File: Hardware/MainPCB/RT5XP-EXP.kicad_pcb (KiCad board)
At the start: 4 copper layers, 153 x 78 mm, 145 parts, among them J1 Conn_Coaxial, J10 Conn_01x02_Male, J11 Conn_01x11_Male, J12 USB_B_Micro, J2 Conn_Coaxial, J3 Conn_Coaxial, J4 Conn_Coaxial, J5 Conn_Coaxial, J6 DB15_Female_HighDensity_Mount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, J7 AudioJack3, J8 Conn_01x21_Male, J9 Conn_01x21_Male, Q1 MMBT3904, Q2 MMBT3904, SW1 SW_Push, SW2 SW_Push, SW3 SW_Push, SW4 SW_Push, U1 THS7374, U10 LMH1980, U11 LMH1980, U12 MC74HC86ADTR2G, U13 TS5A3357, U14 74LVC1G3157, U2 LMH1251MT_NOPB, U3 MAX4887, U4 MAX4887, U5 CP2102N-Axx-xQFN28, U6 ATmega4809-A, U7 LMH1980, U8 MAX4908, U9 74LVC1G3157

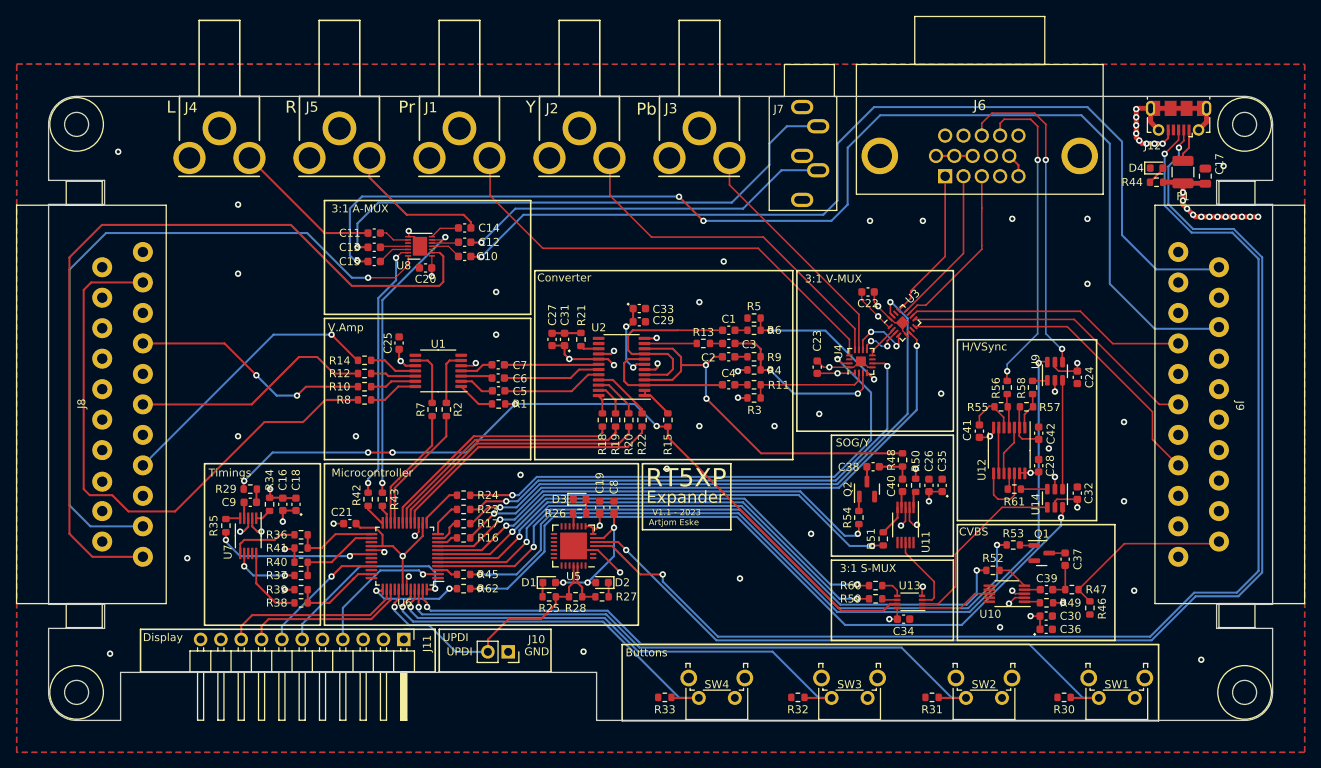
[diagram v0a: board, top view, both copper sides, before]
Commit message: Fixed color bending issue; Added diagnostics
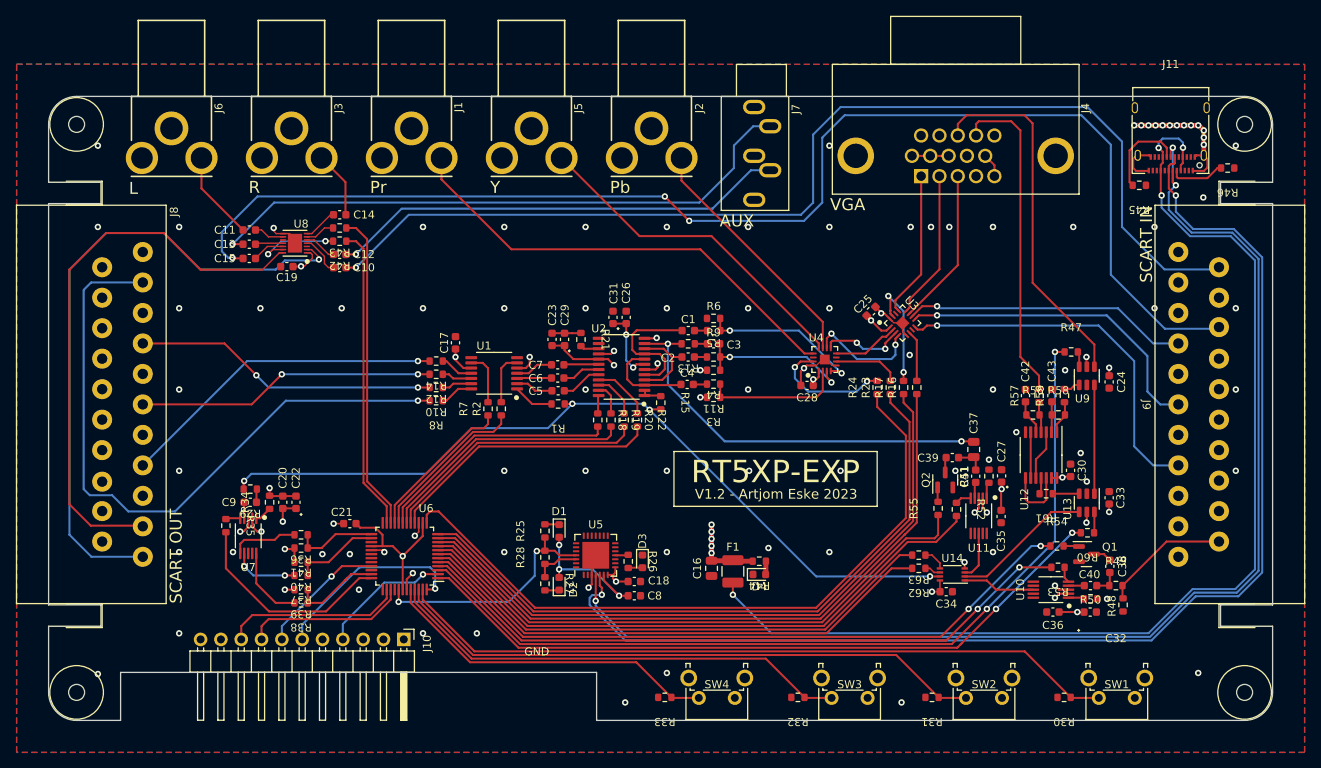
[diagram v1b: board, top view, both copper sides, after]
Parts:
- removed the J10 at (61.4, 73.4)
- removed J12: USB_B_Micro, Connector_USB:USB_Micro-B_Molex-105017-0001
- removed the R48 at (110.7, 49.4)
- added C37: 100uF, Capacitor_SMD:C_0805_2012Metric, F.Cu at (119.6, 48.1)
- added J11: USB-C_12401610E4, RT5XP-EXP:USB-C_12401610E4, F.Cu at (144.3, 7.85)
- added R45: 5.1K, RT5XP-EXP:R_0603, F.Cu at (140.3, 15.1)
- added R46: 5.1K, RT5XP-EXP:R_0603, F.Cu at (151.4, 13.0)
- C1, C2, C4: value 0.22uF -> 4.7nF
- J1, J2, J3, J5: value Conn_Coaxial -> PJRAN1X1U; footprint Mouser:PJRAN1X1U02AUX -> RT5XP-EXP:PJRAN1X1U
- J4: value Conn_Coaxial -> DB15HD_Female; footprint Mouser:PJRAN1X1U02AUX -> RT5XP-EXP:77HDE15SD1CH4RHNVGA
- J6: value DB15_Female_HighDensity_MountingHoles -> PJRAN1X1U; footprint Mouser:L77HDE15SD1CH4RHNVGA -> RT5XP-EXP:PJRAN1X1U
- J7: value AudioJack3 -> SJ1-3535NG; footprint Connector_Audio:Jack_3.5mm_CUI_SJ1-3535NG_Horizontal -> RT5XP-EXP:SJ1-3535NG
- J8, J9: value Conn_01x21_Male -> SCART_Female; footprint AE:SCART -> RT5XP-EXP:SCART_Female
- R1, R10, R11, R12, R14, R15, R16, R17, R18, R19, R2, R20, R21, R22, R23, R24, R25, R26, R27, R28, R29, R3, R30, R31, R32, R33, R34, R35, R36, R37, R38, R39, R4, R40, R41, R42, R43, R44, R5, R6, R61, R7, R8, R9: footprint Resistor_SMD:R_0603_1608Metric -> RT5XP-EXP:R_0603
- R13: value 200R -> 1K; footprint Resistor_SMD:R_0603_1608Metric -> RT5XP-EXP:R_0603
- R47: renamed from R45; footprint Resistor_SMD:R_0603_1608Metric -> RT5XP-EXP:R_0603
- R48: renamed from R46; footprint Resistor_SMD:R_0603_1608Metric -> RT5XP-EXP:R_0603
- R49: renamed from R47; footprint Resistor_SMD:R_0603_1608Metric -> RT5XP-EXP:R_0603
- R50: renamed from R49; footprint Resistor_SMD:R_0603_1608Metric -> RT5XP-EXP:R_0603
- R51: renamed from R50; footprint Resistor_SMD:R_0603_1608Metric -> RT5XP-EXP:R_0603
- R52: renamed from R51; footprint Resistor_SMD:R_0603_1608Metric -> RT5XP-EXP:R_0603
- R53: renamed from R52; footprint Resistor_SMD:R_0603_1608Metric -> RT5XP-EXP:R_0603
- R54: renamed from R53; footprint Resistor_SMD:R_0603_1608Metric -> RT5XP-EXP:R_0603
- R55: renamed from R54; footprint Resistor_SMD:R_0603_1608Metric -> RT5XP-EXP:R_0603
- R56: renamed from R55; footprint Resistor_SMD:R_0603_1608Metric -> RT5XP-EXP:R_0603
- R57: renamed from R56; footprint Resistor_SMD:R_0603_1608Metric -> RT5XP-EXP:R_0603
- R58: renamed from R57; footprint Resistor_SMD:R_0603_1608Metric -> RT5XP-EXP:R_0603
- R59: renamed from R58; footprint Resistor_SMD:R_0603_1608Metric -> RT5XP-EXP:R_0603
- R60: renamed from R62; footprint Resistor_SMD:R_0603_1608Metric -> RT5XP-EXP:R_0603
- R62: renamed from R59; footprint Resistor_SMD:R_0603_1608Metric -> RT5XP-EXP:R_0603
- R63: renamed from R60; footprint Resistor_SMD:R_0603_1608Metric -> RT5XP-EXP:R_0603
- U1: footprint Package_SO:TSSOP-14_4.4x5mm_P0.65mm -> RT5XP-EXP:TSSOP-14_4.4x5mm_P0.65mm
- U10, U11, U7: footprint Package_SO:VSSOP-10_3x3mm_P0.5mm -> RT5XP-EXP:VSSOP-10_3x3mm_P0.5mm
- U2: footprint Package_SO:TSSOP-24_4.4x7.8mm_P0.65mm -> RT5XP-EXP:TSSOP-24_4.4x7.8mm_P0.65mm
- U3, U4: footprint Package_DFN_QFN:TQFN-16-1EP_3x3mm_P0.5mm_EP1.23x1.23mm -> RT5XP-EXP:TQFN-16-1EP_3x3mm_P0.5mm_EP1.23x1.23mm
- U8: footprint Package_DFN_QFN:TDFN-14-1EP_3x3mm_P0.4mm_EP1.78x2.35mm -> RT5XP-EXP:TDFN-14-1EP_3x3mm_P0.4mm_EP1.78x2.35mm
- moved J6 97.5 mm to (19.4, -3.29), turned to 0 degrees
- moved J4 91.2 mm to (116.5, 5.59), turned to 0 degrees
- moved R47 80.9 mm to (131.8, 35.9)
- moved C16 78.8 mm to (86.9, 63.0), turned to 90 degrees
- moved R60 78.3 mm to (133.9, 58.5)
- moved F1 75.2 mm to (89.5, 63.4), turned to 90 degrees
- moved D4 71.0 mm to (92.8, 63.8)
- moved R44 68.6 mm to (92.8, 62.1), turned to 180 degrees
- moved R16 59.7 mm to (112.5, 40.4), turned to 90 degrees
- moved R17 57.6 mm to (110.9, 40.4), turned to 90 degrees
- moved R23 55.5 mm to (109.2, 40.4), turned to 90 degrees
- moved R24 53.4 mm to (107.6, 40.4), turned to 90 degrees
- moved J3 52.2 mm to (34.4, -3.29), turned to 0 degrees
- moved R43 34.3 mm to (40.4, 20.4), turned to 180 degrees
- moved R42 32.5 mm to (40.4, 22.1), turned to 180 degrees
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- renumbered C17 to C16, C25 to C17, C19 to C18, C20 to C19, C16 to C20, C18 to C22, C27 to C23, C22 to C25, C29 to C26, C26 to C27, C23 to C28, C31 to C29, C28 to C30, C33 to C31, C30 to C32, C32 to C33, C37 to C38, C38 to C39, C39 to C40, C40 to C41, C41 to C42, C42 to C43, J11 to J10, U14 to U13, U13 to U14
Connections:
- net Net-(R13-Pad2) renamed SOG/Y
- J1 pad 3: (no net) -> unconnected-(J1-Pad3)
- J2 pad 1: COMP_Green -> COMP_Blue
- J2 pad 3: (no net) -> unconnected-(J2-Pad3)
- J3 pad 1: COMP_Blue -> RCA_AudioR
- J3 pad 3: (no net) -> unconnected-(J3-Pad3)
- J4 pad 1: RCA_AudioL -> VGA_Red
- J4 pad 2: GND -> VGA_Green
- J4 pad 3: (no net) -> VGA_Blue
- J5 pad 1: RCA_AudioR -> COMP_Green
- J5 pad 3: (no net) -> unconnected-(J5-Pad3)
- J6 pad 1: VGA_Red -> RCA_AudioL
- J6 pad 2: VGA_Green -> GND
- J6 pad 3: VGA_Blue -> unconnected-(J6-Pad3)
- J8 pad 14: unconnected-(J8-Pad14) -> GND
- J9 pad 14: unconnected-(J9-Pad14) -> GND
- U6 pad 1: unconnected-(U6-Pad1) -> MCU_CMUX
- U6 pad 20: unconnected-(U6-Pad20) -> MCU_AMP_DIS
- U6 pad 21: MCU_AMP_DIS -> MCU_AMP_BY
- U6 pad 22: MCU_AMP_BY -> MCU_4908_1
- U6 pad 23: MCU_4908_1 -> MCU_4908_2
- U6 pad 24: MCU_4908_2 -> unconnected-(U6-Pad24)
- U6 pad 30: MCU_HD -> unconnected-(U6-Pad30)
- U6 pad 36: unconnected-(U6-Pad36) -> MCU_HD
- U6 pad 37: MCU_CMUX -> unconnected-(U6-Pad37)
- U6 pad 4: MCU_SCARTC_FILTER -> MCU_SCARTC_HD
- U6 pad 5: MCU_SCARTC_HD -> MCU_SCARTC_FILTER
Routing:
- net VBUS: track 4.18 -> 140.7 mm, vias 0 -> 4
- net MCU_VGAMUX: track 2.60 -> 111.1 mm, vias 0 -> 2
- net Net-(R47-Pad2): track 108.4 -> 1.92 mm, vias 2 -> 0
- net Net-(R60-Pad1): track 92.6 -> 2.62 mm, vias 2 -> 0
- net MCU_MAX4887_EN: track 2.60 -> 84.8 mm
- net MCU_MAX4887/2_SEL: track 5.59 -> 87.7 mm
- net MCU_MAX4887_SEL: track 3.53 -> 84.6 mm
- net MCU_MAX4887/2_EN: track 4.49 -> 84.4 mm
- net MCU_CMUX: track 11.9 -> 90.1 mm
- net Net-(R16-Pad2): track 72.6 -> 6.41 mm, vias 2 -> 0
- net Net-(R17-Pad2): track 77.2 -> 14.2 mm
- net Net-(R23-Pad2): track 66.2 -> 8.40 mm, vias 2 -> 0
- net Net-(R24-Pad2): track 66.5 -> 15.5 mm
- net SOG/Y: track 6.46 -> 50.9 mm, vias 0 -> 2
- net VGA/SCART/COMP_Green_75: track 48.8 -> 10.6 mm, vias 2 -> 0
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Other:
- outline, holes or cut-outs redrawn
- board text added: "AUX"
- board text added: "RT5XP-EXP"
- board text added: "SCART IN"
- board text added: "SCART OUT"
- board text added: "V1.2 - Artjom Eske 2023"
- board text added: "VGA"
- board text removed: "3:1 A-MUX"
- board text removed: "3:1 S-MUX"
- board text removed: "3:1 V-MUX"
- board text removed: "Artjom Eske"
- board text removed: "Buttons"
- board text removed: "CVBS"
- board text removed: "Converter"
- board text removed: "Display"
- board text removed: "Expander"
- board text removed: "H/VSync"
- board text removed: "Microcontroller"
- board text removed: "RT5XP"
- board text removed: "SOG/Y"
- board text removed: "Timings"
- board text removed: "UPDI"
- board text removed: "V.Amp"
- board text removed: "V1.1 - 2023"
